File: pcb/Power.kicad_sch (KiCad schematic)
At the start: 35 parts, among them J3 24v Input, Q1 DMP3013SFV-7, U7 AP64501SP-13, U8 LT1761-3.3

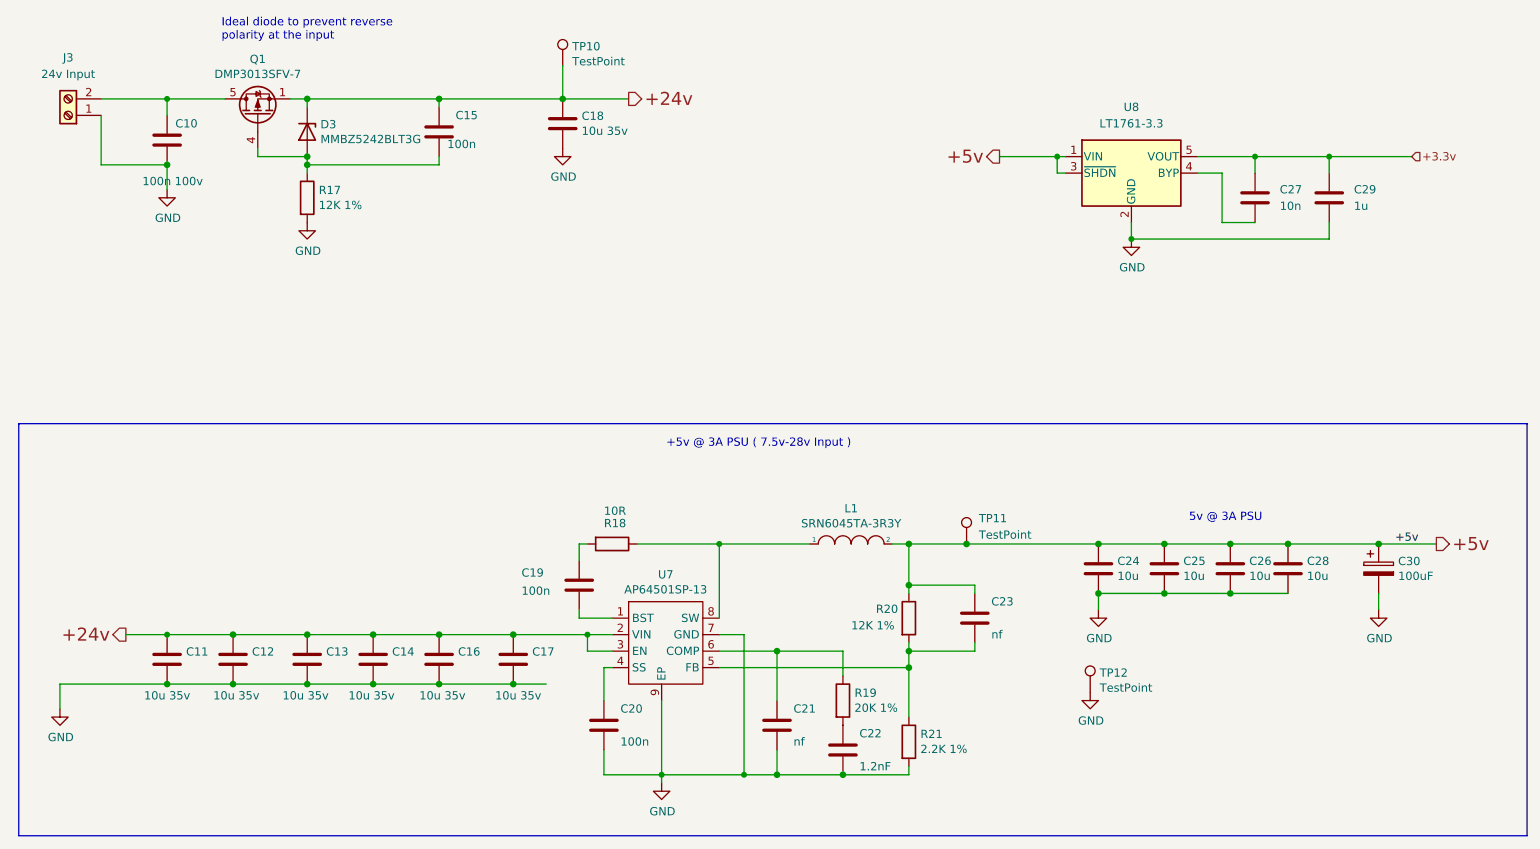
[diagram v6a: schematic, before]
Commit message: - work in progress, changed rj45 connector
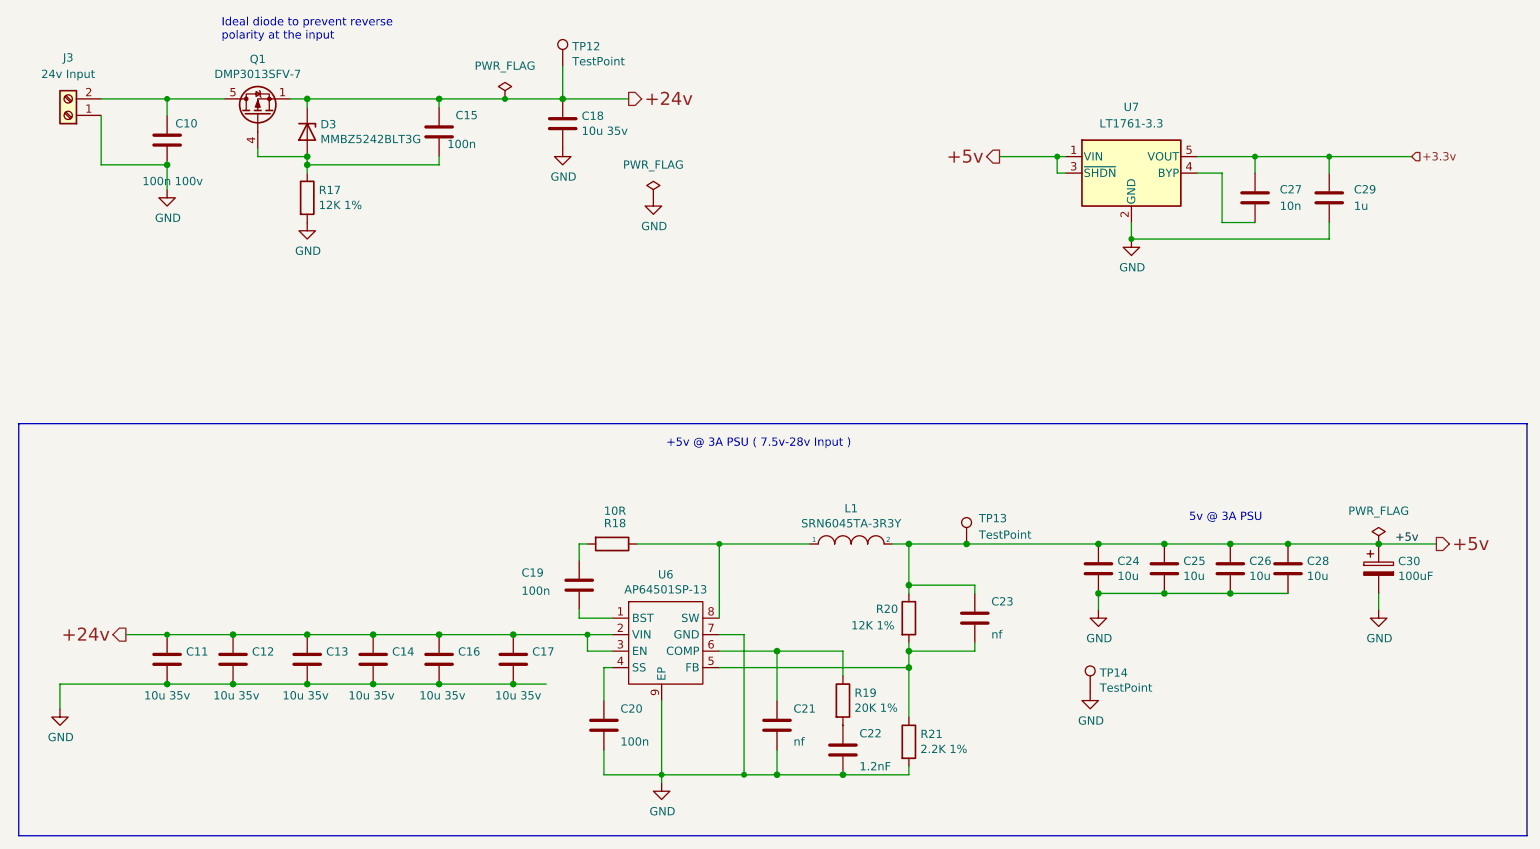
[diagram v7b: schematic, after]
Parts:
- renumbered TP10 to TP12, TP11 to TP13, TP12 to TP14, U7 to U6, U8 to U7

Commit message: - component selection/place
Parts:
- TP16: renamed from TP13; footprint TestPoint:TestPoint_Bridge_Pitch2.54mm_Drill1.0mm -> TestPoint:TestPoint_Bridge_Pitch2.0mm_Drill0.7mm
- TP17: renamed from TP14; footprint TestPoint:TestPoint_Bridge_Pitch2.54mm_Drill1.0mm -> TestPoint:TestPoint_Bridge_Pitch2.0mm_Drill0.7mm
- renumbered C10 to C13, C11 to C14, C12 to C15, C13 to C16, C14 to C17, C15 to C18, C16 to C19, C17 to C20, C18 to C21, C19 to C22, C20 to C23, C21 to C24, C22 to C25, C23 to C26, C24 to C27, C25 to C28, C26 to C29, C27 to C30, C28 to C31, C29 to C32, C30 to C33, R17 to R18, R18 to R19, R19 to R20, R20 to R21, R21 to R22, TP12 to TP15
